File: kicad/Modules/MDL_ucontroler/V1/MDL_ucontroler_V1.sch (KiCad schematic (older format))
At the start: 1 part

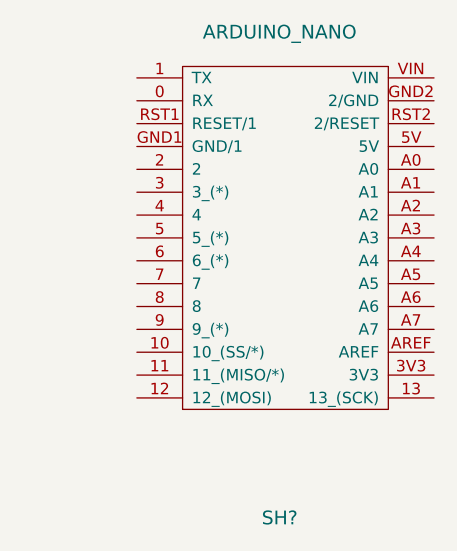
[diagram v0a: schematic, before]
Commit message: adding module software
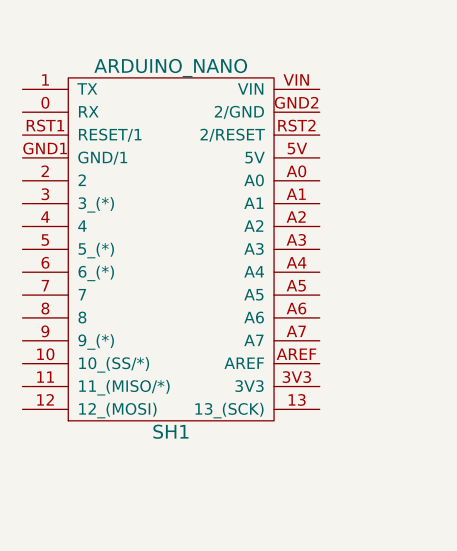
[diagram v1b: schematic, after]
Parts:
- removed SH?: ARDUINO_NANO, symbol ARDUINO_NANO
- added SH1: ARDUINO_NANO, symbol ARDUINO_NANO
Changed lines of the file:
@@
 EESchema Schematic File Version 2
+LIBS:MDL_ucontroler_V1-rescue
 LIBS:power
 LIBS:device
@@
 LIBS:valves
 LIBS:echopen
+LIBS:MDL_ucontroler_V1-cache
 EELAYER 25 0
 EELAYER END
@@
 $EndDescr
 $Comp
-L ARDUINO_NANO SH?
-U 1 1 57A4F44C
-P 5650 3150
-F 0 "SH?" H 5625 2075 60  0000 C CNN
-F 1 "ARDUINO_NANO" H 5625 4200 60  0000 C CNN
-F 2 "" H 4725 2550 60  0000 C CNN
-F 3 "" H 4725 2550 60  0000 C CNN
-	1    5650 3150
+L ARDUINO_NANO SH1
+U 1 1 57AAFAD2
+P 5150 3200
+F 0 "SH1" H 5150 2550 60  0000 C CNN
+F 1 "ARDUINO_NANO" H 5150 4150 60  0000 C CNN
+F 2 "" H 4225 2600 60  0000 C CNN
+F 3 "" H 4225 2600 60  0000 C CNN
+	1    5150 3200
 	1    0    0    -1
 $EndComp
